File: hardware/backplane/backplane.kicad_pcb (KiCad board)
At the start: 2 copper layers, 200 x 124 mm, 86 parts, among them J1 C96ABC, J10 Conn_Coaxial_Power, J2 C96ABC, J3 C96ABC, J4 C96ABC, J5 C96ABC, J6 C96ABC, J7 C96ABC, J8 C96ABC, J9 C96ABC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

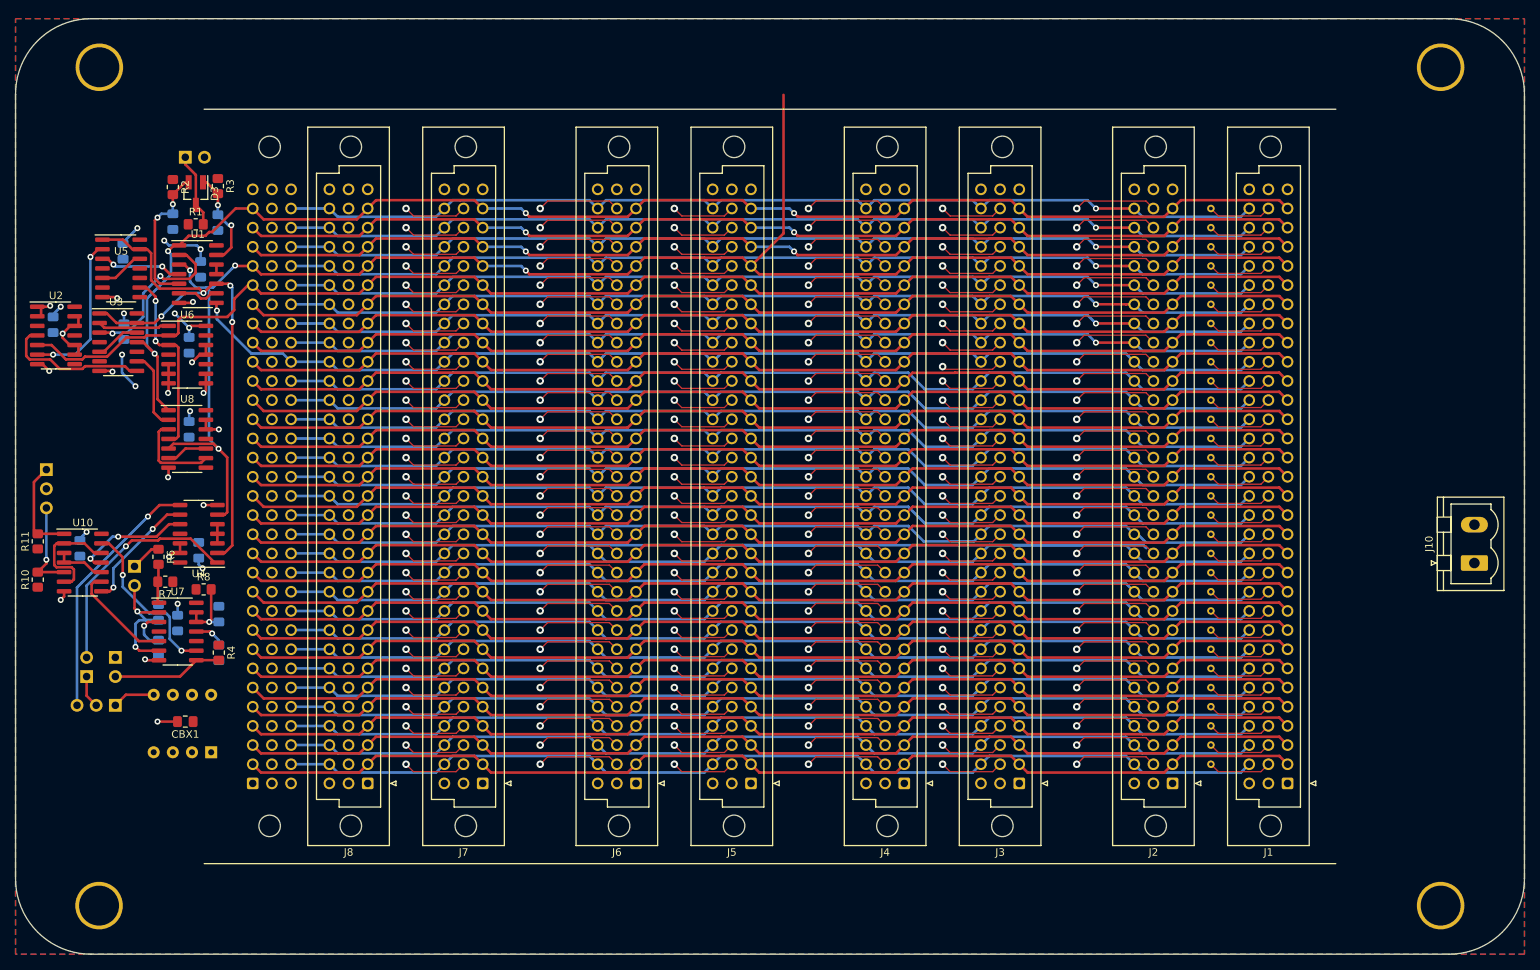
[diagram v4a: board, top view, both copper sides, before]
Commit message: backplane: add soft power on/off circuit to backplane
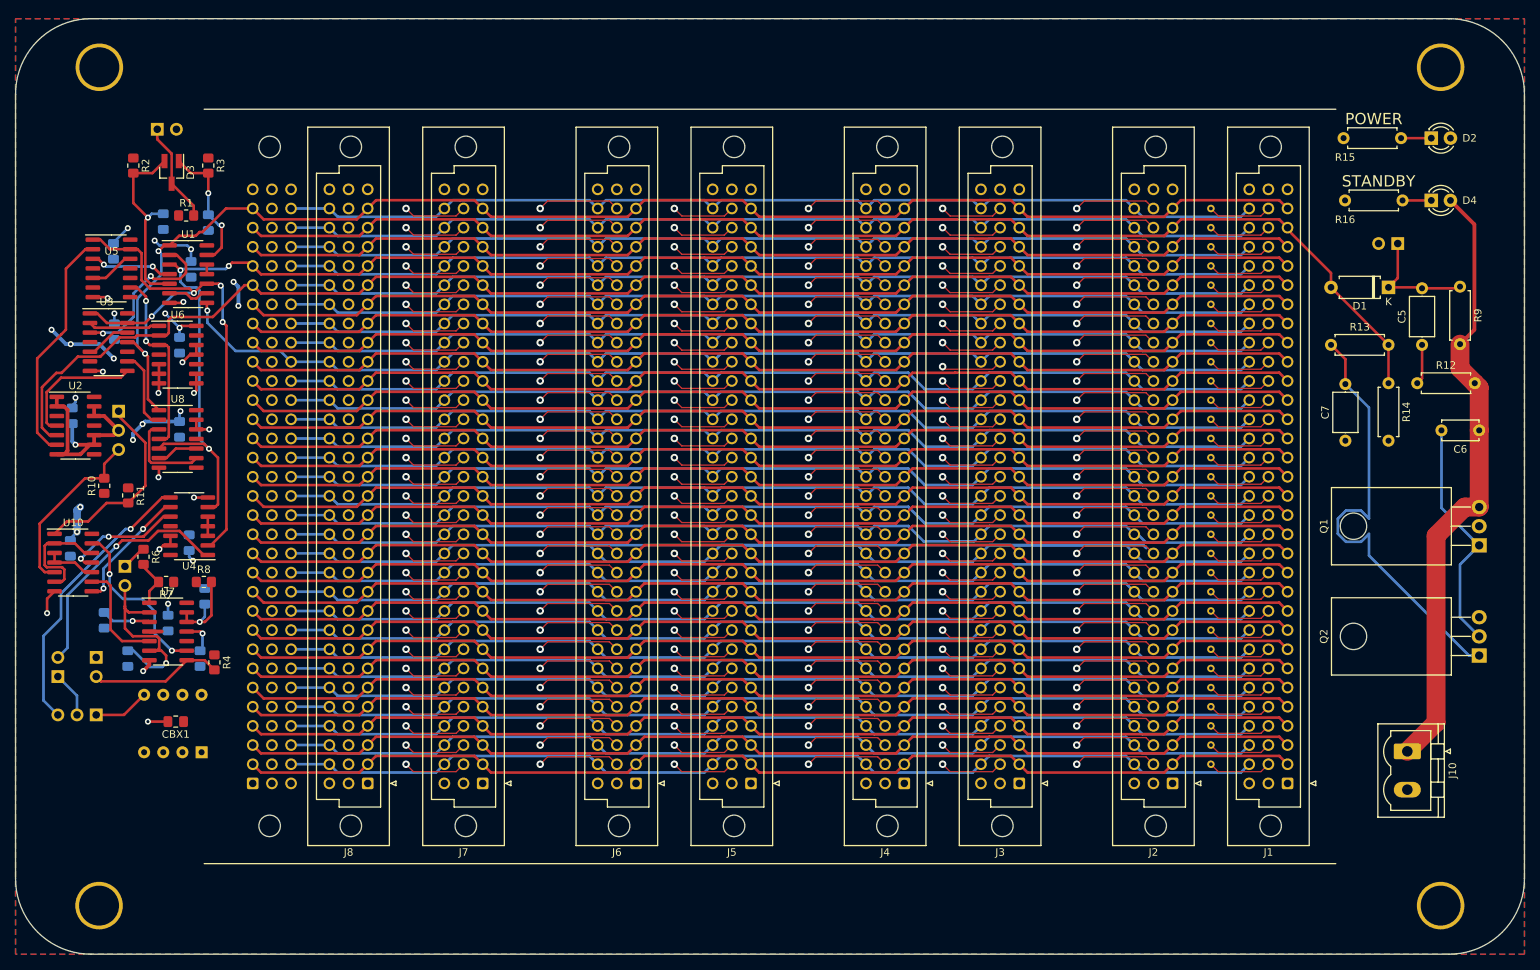
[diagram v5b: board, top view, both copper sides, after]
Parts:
- added C5: 1uF, Capacitor_THT:C_Axial_L5.1mm_D3.1mm_P7.50mm_Horizontal, F.Cu at (230.5, 71.8)
- added C6: 0.1uF, Capacitor_THT:C_Disc_D4.7mm_W2.5mm_P5.00mm, F.Cu at (238.1, 83.1)
- added C7: 10uF, Capacitor_THT:C_Axial_L5.1mm_D3.1mm_P7.50mm_Horizontal, F.Cu at (220.3, 84.5)
- added D1: BAT54J, Diode_THT:D_A-405_P7.62mm_Horizontal, F.Cu at (226.1, 64.1)
- added D2: LED, LED_THT:LED_D3.0mm, F.Cu at (231.7, 44.4)
- added D4: LED, LED_THT:LED_D3.0mm, F.Cu at (231.7, 52.6)
- added JPC2: JP_PWR_BTN, Connector_PinHeader_2.54mm:PinHeader_1x02_P2.54mm_Vertical, B.Cu at (227.3, 58.3)
- added Q1: FQP27P06, Package_TO_SOT_THT:TO-220-3_Horizontal_TabDown, F.Cu at (238.1, 98.3)
- added Q2: BUZ11, Package_TO_SOT_THT:TO-220-3_Horizontal_TabDown, F.Cu at (238.1, 112.9)
- added R12: 100k, Resistor_THT:R_Axial_DIN0207_L6.3mm_D2.5mm_P7.62mm_Horizontal, F.Cu at (229.9, 76.8)
- added R13: 300k, Resistor_THT:R_Axial_DIN0207_L6.3mm_D2.5mm_P7.62mm_Horizontal, F.Cu at (218.4, 71.8)
- added R14: 100k, Resistor_THT:R_Axial_DIN0207_L6.3mm_D2.5mm_P7.62mm_Horizontal, F.Cu at (226.1, 76.8)
- added R15: 1k, Resistor_THT:R_Axial_DIN0207_L6.3mm_D2.5mm_P7.62mm_Horizontal, F.Cu at (220.1, 44.4)
- added R16: 1k, Resistor_THT:R_Axial_DIN0207_L6.3mm_D2.5mm_P7.62mm_Horizontal, F.Cu at (220.3, 52.6)
- added R9: 10k, Resistor_THT:R_Axial_DIN0207_L6.3mm_D2.5mm_P7.62mm_Horizontal, F.Cu at (235.5, 64.0)
- moved J10 26.5 mm to (228.6, 125.6), turned to 270 degrees
- moved R10 15.2 mm to (55.8, 90.4)
- moved R11 13.4 mm to (59.0, 91.7), turned to 270 degrees
- moved CBU2 12.3 mm to (51.6, 81.2)
- moved SW3 12.3 mm to (57.7, 80.5)
- moved U2 12.2 mm to (52.0, 82.5)
- moved C1 8.07 mm to (55.8, 108.3)
- moved C3 7.34 mm to (59.0, 113.3), turned to 270 degrees
- moved R2 5.96 mm to (59.7, 48.0)
- moved JPC1 5.25 mm to (62.9, 43.2)
- moved D3 4.27 mm to (64.8, 48.9)
- moved JP1 3.81 mm to (49.7, 115.7)
- moved R3 3.00 mm to (69.6, 48.0)
- moved C4 3.00 mm to (69.2, 105.1)
- moved SW2 2.84 mm to (54.8, 120.8)
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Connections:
- J10 pad 1: VCC -> +5V
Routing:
- net +5V: track 0.00 -> 81.2 mm
- net Net-(C7-Pad2): track 0.00 -> 60.1 mm
- net Net-(C6-Pad2): track 0.00 -> 31.5 mm
- net A30: track 144.5 -> 170.6 mm, vias 2 -> 0
- net A28: track 221.6 -> 198.9 mm, vias 4 -> 3
- net GND: track 42.8 -> 63.4 mm, vias 16 -> 14
- net VCC: track 30.1 -> 50.7 mm, vias 13 -> 19
- net Net-(C5-Pad2): track 0.00 -> 15.9 mm
- net Net-(R11-Pad2): track 12.9 -> 26.0 mm
- net Net-(R10-Pad2): track 12.5 -> 23.6 mm, vias 1 -> 0
- net Net-(U2-Pad6): track 20.8 -> 31.9 mm, vias 2 -> 0
- net A27: track 179.7 -> 187.4 mm
- net Net-(C3-Pad1): track 19.4 -> 27.0 mm, vias 2 -> 1
- net Net-(CR1-Pad1): track 19.3 -> 25.5 mm, vias 2 -> 1
- net Net-(C5-Pad1): track 0.00 -> 5.34 mm
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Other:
- net class Power added: clearance 0.15, trace_width 0.5, via_dia 0.8, via_drill 0.4
- board text added: "POWER"
- board text added: "RESET"
- board text added: "STANDBY"

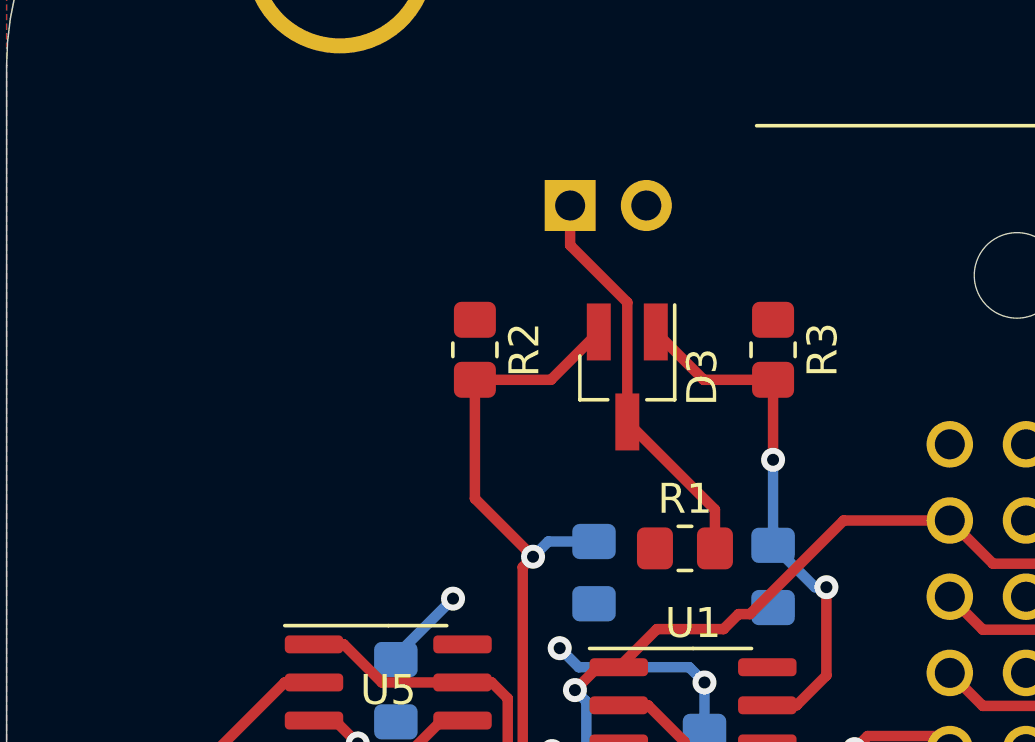
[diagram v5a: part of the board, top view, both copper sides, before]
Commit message: backplane: make some diodes through hole
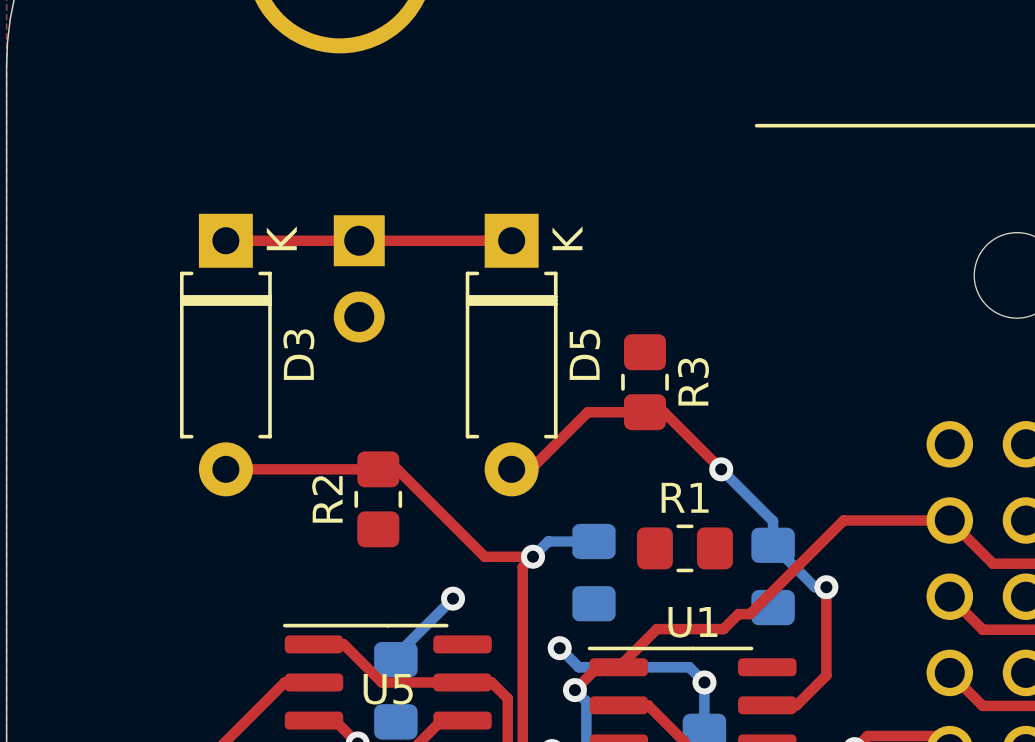
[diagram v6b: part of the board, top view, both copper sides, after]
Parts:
- added D5: BAT54J, Diode_THT:D_A-405_P7.62mm_Horizontal, F.Cu at (60.9, 44.4)
- D3: value D_Schottky_x2_KCom_AAK -> BAT54J; footprint Package_TO_SOT_SMD:SOT-23_Handsoldering -> Diode_THT:D_A-405_P7.62mm_Horizontal
- moved D3 14.1 mm to (51.4, 44.4)
- moved JPC1 7.13 mm to (55.8, 44.4), turned to 180 degrees
- moved R2 5.93 mm to (56.5, 53.0), turned to 90 degrees
- moved R3 4.40 mm to (65.4, 49.1)
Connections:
- D3 pad 1: Net-(CR2-Pad1) -> ~RST_HDR~
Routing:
- net ~RST_HDR~: track 13.4 -> 9.52 mm
- net Net-(CR2-Pad1): track 17.8 -> 19.5 mm

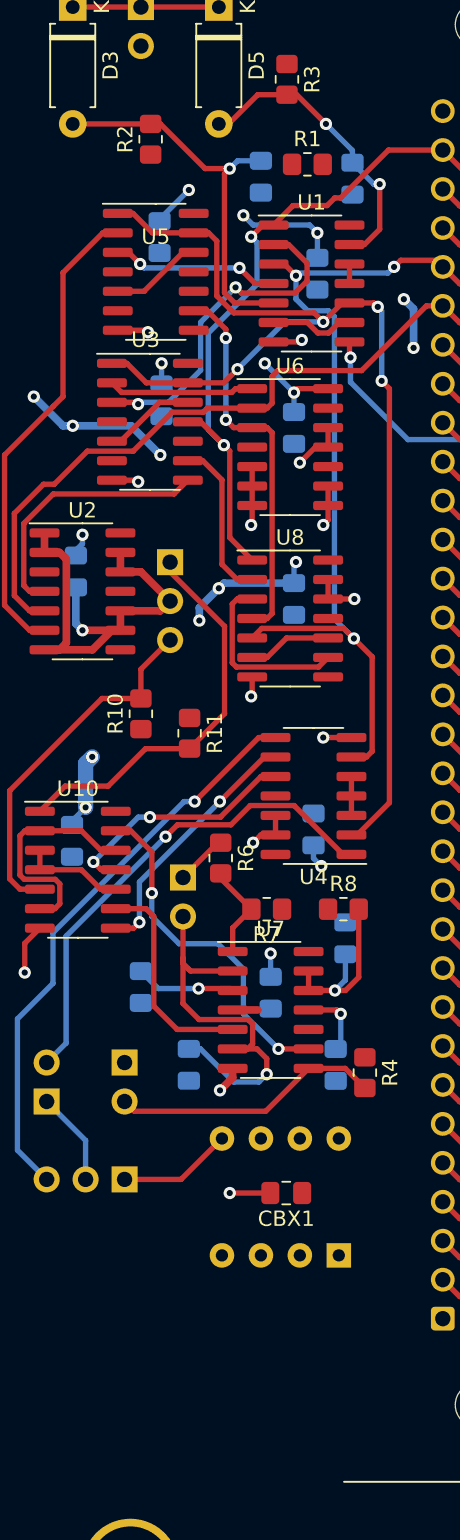
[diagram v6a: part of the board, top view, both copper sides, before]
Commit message: backplane: add a logo
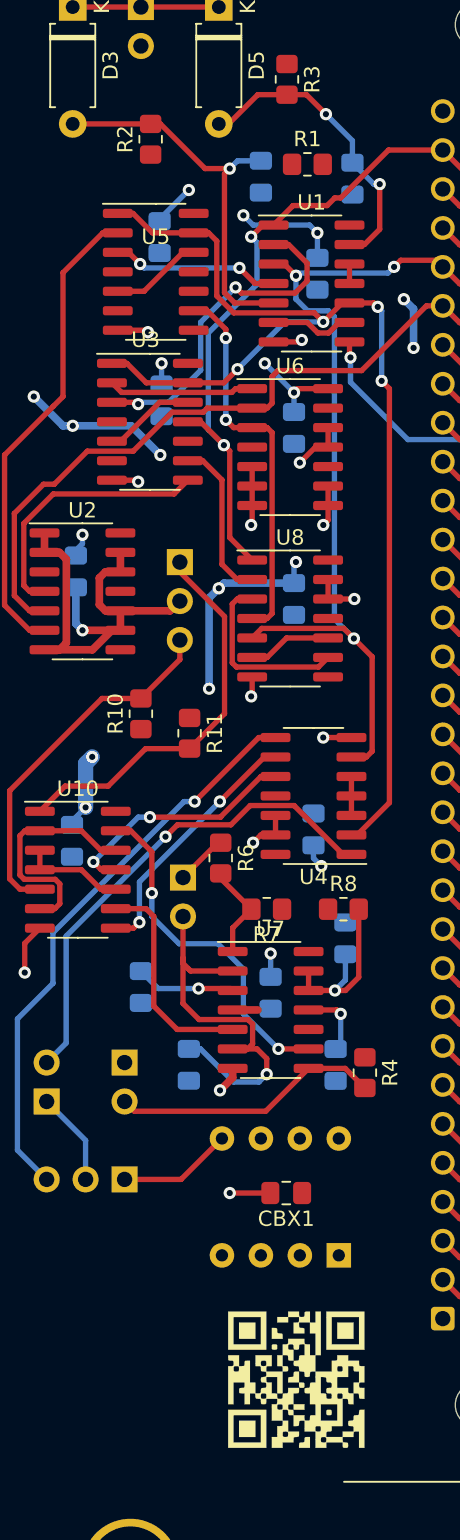
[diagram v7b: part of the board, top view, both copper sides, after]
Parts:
- added G***: LOGO, graphics:qr_code, F.Cu at (66.0, 133.9)
- added G***: LOGO, graphics:microclem_logo_mask, F.Cu at (53.3, 132.0)
- moved SW3 0.63 mm to (58.4, 80.5)
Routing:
- net VCC: track 50.7 -> 54.9 mm
- net GND: track 63.4 -> 64.9 mm
